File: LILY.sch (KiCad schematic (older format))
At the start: 8 parts

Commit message: LILY notitzen hinzugefügt
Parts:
- added C?: C, symbol C
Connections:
- net labels added: +3.3V, HOST_WKUP, POWER_DOWN-N, SDIO_EN-N, WAKE_UP
- wire segments 18 -> 24
- no-connect marks 6 -> 8
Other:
- note added: "Output wake up signal to host. \n\n"
- note added: "Pin is also used by USB as USB_VBUS_ON: \nUSB VBus On, USB power valid indication. \n"
- note added: "USB/SDIO-n :High level activates the USB interface. Internal pull-up (USB is default). Notice 1.8 V pin. \n"
- note added: "Wake up input signal. Active high .Notice 1.8 V pin. \n\n\n"
- moved on the sheet: C?, R?, U?
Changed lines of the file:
@@
 L R R?
 U 1 1 57112774
-P 6050 3950
-F 0 "R?" V 6130 3950 50  0000 C CNN
-F 1 "R" V 5975 3950 50  0000 C CNN
-F 2 "" V 5980 3950 30  0000 C CNN
-F 3 "" H 6050 3950 30  0000 C CNN
-	1    6050 3950
+P 6050 4100
+F 0 "R?" V 6130 4100 50  0000 C CNN
+F 1 "R" V 5975 4100 50  0000 C CNN
+F 2 "" V 5980 4100 30  0000 C CNN
+F 3 "" H 6050 4100 30  0000 C CNN
+	1    6050 4100
 	0    1    1    0
 $EndComp
@@
 L R R?
 U 1 1 571127A8
-P 5450 4050
-F 0 "R?" V 5530 4050 50  0000 C CNN
-F 1 "R" V 5375 4050 50  0000 C CNN
-F 2 "" V 5380 4050 30  0000 C CNN
-F 3 "" H 5450 4050 30  0000 C CNN
-	1    5450 4050
+P 5450 4200
+F 0 "R?" V 5530 4200 50  0000 C CNN
+F 1 "R" V 5375 4200 50  0000 C CNN
+F 2 "" V 5380 4200 30  0000 C CNN
+F 3 "" H 5450 4200 30  0000 C CNN
+	1    5450 4200
 	0    1    1    0
 $EndComp
@@
 L C C?
 U 1 1 571127D2
-P 6400 4450
-F 0 "C?" H 6450 4550 50  0000 L CNN
-F 1 "C" H 6450 4350 50  0000 L CNN
-F 2 "" H 6438 4300 30  0000 C CNN
-F 3 "" H 6450 4550 60  0000 C CNN
-	1    6400 4450
+P 6400 4600
+F 0 "C?" H 6450 4700 50  0000 L CNN
+F 1 "C" H 6450 4500 50  0000 L CNN
+F 2 "" H 6438 4450 30  0000 C CNN
+F 3 "" H 6450 4700 60  0000 C CNN
+	1    6400 4600
 	1    0    0    -1
 $EndComp
@@
 L C C?
 U 1 1 571127FC
-P 6800 4450
-F 0 "C?" H 6850 4550 50  0000 L CNN
-F 1 "C" H 6850 4350 50  0000 L CNN
-F 2 "" H 6838 4300 30  0000 C CNN
-F 3 "" H 6850 4550 60  0000 C CNN
-	1    6800 4450
-	1    0    0    -1
-$EndComp
-Wire Wire Line
-	4900 3950 5850 3950
-Wire Wire Line
-	5250 4050 4900 4050
-Wire Wire Line
-	5650 4050 7150 4050
-Wire Wire Line
-	6400 4050 6400 4250
-Wire Wire Line
-	6250 3950 7150 3950
-Wire Wire Line
-	6800 3950 6800 4250
-Connection ~ 6400 4050
-Connection ~ 6800 3950
+P 6800 4600
+F 0 "C?" H 6850 4700 50  0000 L CNN
+F 1 "C" H 6850 4500 50  0000 L CNN
+F 2 "" H 6838 4450 30  0000 C CNN
+F 3 "" H 6850 4700 60  0000 C CNN
+	1    6800 4600
+	1    0    0    -1
+$EndComp
+Wire Wire Line
+	4900 4100 5850 4100
+Wire Wire Line
+	5250 4200 4900 4200
+Wire Wire Line
+	5650 4200 7150 4200
+Wire Wire Line
+	6400 4200 6400 4400
+Wire Wire Line
+	6250 4100 7150 4100
+Wire Wire Line
+	6800 4100 6800 4400
+Connection ~ 6400 4200
+Connection ~ 6800 4100
 $Comp
 L GND #PWR?
 U 1 1 57112915
-P 6800 4800
-F 0 "#PWR?" H 6800 4550 50  0001 C CNN
-F 1 "GND" H 6800 4650 50  0000 C CNN
-F 2 "" H 6800 4800 50  0000 C CNN
-F 3 "" H 6800 4800 50  0000 C CNN
-	1    6800 4800
+P 6800 4950
+F 0 "#PWR?" H 6800 4700 50  0001 C CNN
+F 1 "GND" H 6800 4800 50  0000 C CNN
+F 2 "" H 6800 4950 50  0000 C CNN
+F 3 "" H 6800 4950 50  0000 C CNN
+	1    6800 4950
 	1    0    0    -1
 $EndComp
@@
 L GND #PWR?
 U 1 1 5711293E
-P 6400 4800
-F 0 "#PWR?" H 6400 4550 50  0001 C CNN
-F 1 "GND" H 6400 4650 50  0000 C CNN
-F 2 "" H 6400 4800 50  0000 C CNN
-F 3 "" H 6400 4800 50  0000 C CNN
-	1    6400 4800
-	1    0    0    -1
-$EndComp
-Wire Wire Line
-	6800 4800 6800 4650
-Wire Wire Line
-	6400 4650 6400 4800
-Text HLabel 7150 4050 2    60   Input ~ 0
+P 6400 4950
+F 0 "#PWR?" H 6400 4700 50  0001 C CNN
+F 1 "GND" H 6400 4800 50  0000 C CNN
+F 2 "" H 6400 4950 50  0000 C CNN
+F 3 "" H 6400 4950 50  0000 C CNN
+	1    6400 4950
+	1    0    0    -1
+$EndComp
+Wire Wire Line
+	6800 4950 6800 4800
+Wire Wire Line
+	6400 4800 6400 4950
+Text HLabel 7150 4200 2    60   Input ~ 0
 USB_D+
-Text HLabel 7150 3950 2    60   Input ~ 0
+Text HLabel 7150 4100 2    60   Input ~ 0
 USB_D-
 $Comp
 L AS179-92LF U?
 U 1 1 57112CC8
-P 7800 2850
-F 0 "U?" H 8050 2600 60  0000 C CNN
-F 1 "AS179-92LF" H 7800 3100 60  0000 C CNN
-F 2 "" H 7850 2850 60  0000 C CNN
-F 3 "" H 7850 2850 60  0000 C CNN
-	1    7800 2850
+P 8600 3300
+F 0 "U?" H 8850 3050 60  0000 C CNN
+F 1 "AS179-92LF" H 8600 3550 60  0000 C CNN
+F 2 "" H 8650 3300 60  0000 C CNN
+F 3 "" H 8650 3300 60  0000 C CNN
+	1    8600 3300
 	1    0    0    -1
 $EndComp
@@
 L R R?
 U 1 1 57112D8E
-P 6050 2700
-F 0 "R?" V 6130 2700 50  0000 C CNN
-F 1 "R" V 5975 2700 50  0000 C CNN
-F 2 "" V 5980 2700 30  0000 C CNN
-F 3 "" H 6050 2700 30  0000 C CNN
-	1    6050 2700
+P 6850 3150
+F 0 "R?" V 6930 3150 50  0000 C CNN
+F 1 "R" V 6775 3150 50  0000 C CNN
+F 2 "" V 6780 3150 30  0000 C CNN
+F 3 "" H 6850 3150 30  0000 C CNN
+	1    6850 3150
 	0    1    1    0
 $EndComp
@@
 L R R?
 U 1 1 57112DE1
-P 6500 2850
-F 0 "R?" V 6580 2850 50  0000 C CNN
-F 1 "R" V 6425 2850 50  0000 C CNN
-F 2 "" V 6430 2850 30  0000 C CNN
-F 3 "" H 6500 2850 30  0000 C CNN
-	1    6500 2850
-	0    1    1    0
-$EndComp
-Wire Wire Line
-	7300 2700 6250 2700
-Wire Wire Line
-	6700 2850 7300 2850
-Wire Wire Line
-	4900 3100 5650 3100
-Wire Wire Line
-	5650 3100 5650 2700
-Wire Wire Line
-	5650 2700 5850 2700
-Wire Wire Line
-	4900 3200 5750 3200
-Wire Wire Line
-	5750 3200 5750 2850
-Wire Wire Line
-	5750 2850 6300 2850
+P 7300 3300
+F 0 "R?" V 7380 3300 50  0000 C CNN
+F 1 "R" V 7225 3300 50  0000 C CNN
+F 2 "" V 7230 3300 30  0000 C CNN
+F 3 "" H 7300 3300 30  0000 C CNN
+	1    7300 3300
+	0    1    1    0
+$EndComp
+Wire Wire Line
+	8100 3150 7050 3150
+Wire Wire Line
+	7500 3300 8100 3300
+Wire Wire Line
+	4900 3250 5650 3250
+Wire Wire Line
+	4900 3350 5750 3350
+Text HLabel 2650 2550 0    60   Input ~ 0
+WAKE_UP
+Text HLabel 2650 2650 0    60   Input ~ 0
+HOST_WKUP
+Wire Wire Line
+	2650 2550 2900 2550
+Wire Wire Line
+	2650 2650 2900 2650
+Text HLabel 5200 3800 2    60   Input ~ 0
+SDIO_EN-N
+Text HLabel 5200 3900 2    60   Input ~ 0
+POWER_DOWN-N
+$Comp
+L +3.3V #PWR?
+U 1 1 57149C0A
+P 5700 1850
+F 0 "#PWR?" H 5700 1700 50  0001 C CNN
+F 1 "+3.3V" H 5700 1990 50  0000 C CNN
+F 2 "" H 5700 1850 50  0000 C CNN
+F 3 "" H 5700 1850 50  0000 C CNN
+	1    5700 1850
+	1    0    0    -1
+$EndComp
+Wire Wire Line
+	4900 3800 5200 3800
+Wire Wire Line
+	4900 3900 5200 3900
+$Comp
+L GND #PWR?
+U 1 1 5714A025
+P 5700 2800
+F 0 "#PWR?" H 5700 2550 50  0001 C CNN
+F 1 "GND" H 5700 2650 50  0000 C CNN
+F 2 "" H 5700 2800 50  0000 C CNN
+F 3 "" H 5700 2800 50  0000 C CNN
+	1    5700 2800
+	1    0    0    -1
+$EndComp
+$Comp
+L C C?
+U 1 1 5714A0A3
+P 5700 2350
+F 0 "C?" H 5750 2450 50  0000 L CNN
+F 1 "C" H 5750 2250 50  0000 L CNN
+F 2 "" H 5738 2200 30  0000 C CNN
+F 3 "" H 5750 2450 60  0000 C CNN
+	1    5700 2350
+	1    0    0    -1
+$EndComp
+Wire Wire Line
+	4900 2550 5350 2550
+Wire Wire Line
+	5350 1950 5350 2650
+Wire Wire Line
+	5350 1950 5700 1950
+Wire Wire Line
+	5700 1850 5700 2150
+Connection ~ 5700 1950
+Wire Wire Line
+	5700 2800 5700 2550
+Wire Wire Line
+	5350 2650 4900 2650
+Connection ~ 5350 2550
+Text Notes 6000 3800 0    60   ~ 0
+USB/SDIO-n :High level activates the USB interface. Internal pull-up (USB is default). Notice 1.8 V pin. \n
+NoConn ~ 4900 3550
+NoConn ~ 4900 3650
+Text Notes 650  2600 0    60   ~ 0
+Wake up input signal. Active high .Notice 1.8 V pin. \n\n\n
+Text Notes 550  2800 0    60   ~ 0
+Output wake up signal to host. \n\n
+Text Notes 750  3800 0    60   ~ 0
+Pin is also used by USB as USB_VBUS_ON: \nUSB VBus On, USB power valid indication. \n
 $EndSCHEMATC

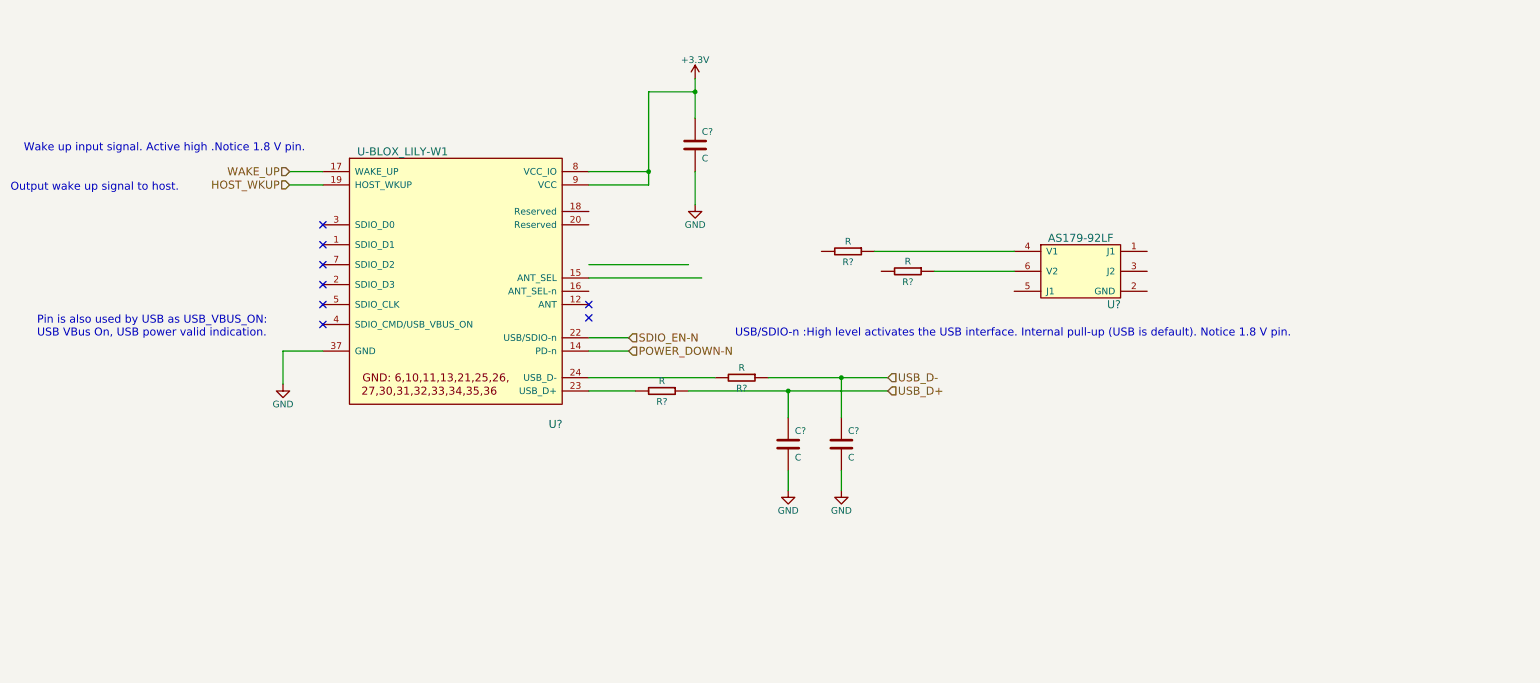
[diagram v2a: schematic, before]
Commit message: 3V8 footprints ergänzt
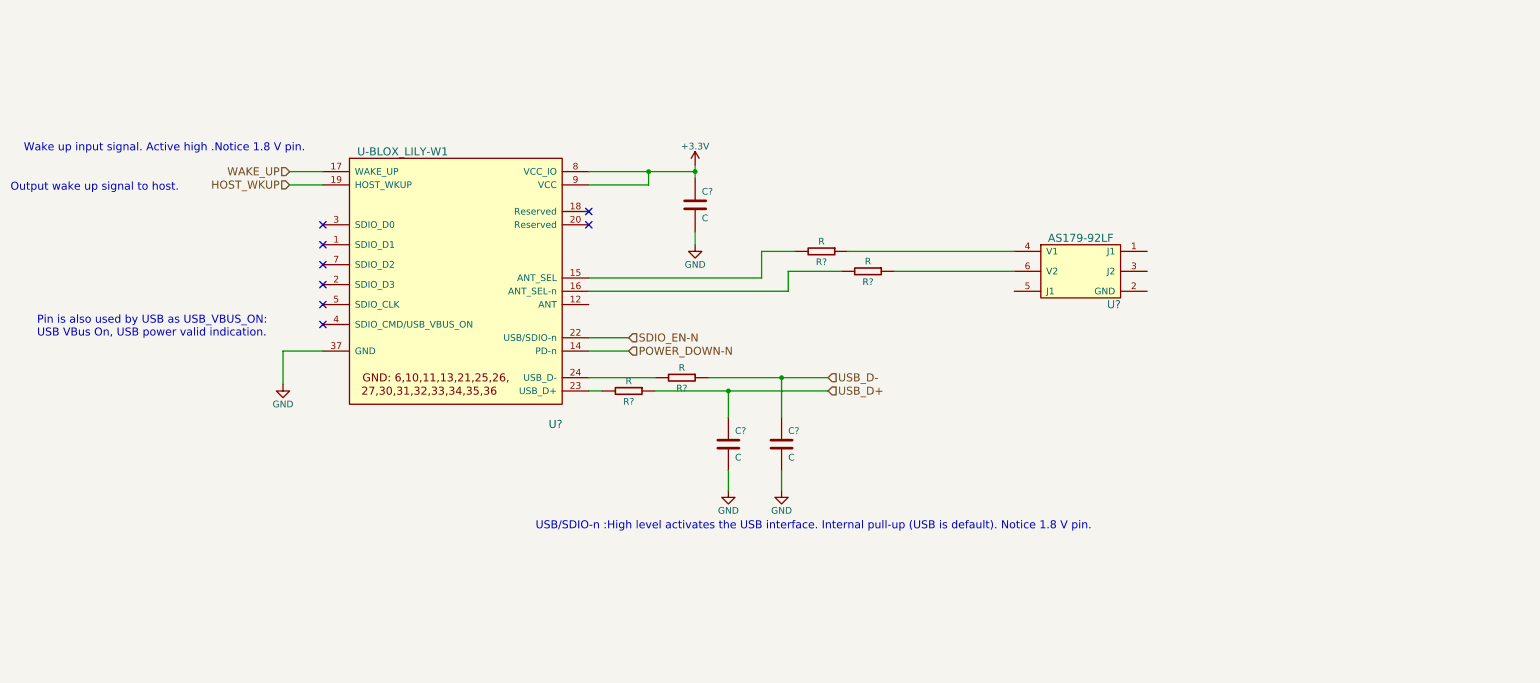
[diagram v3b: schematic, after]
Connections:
- wire segments 24 -> 27
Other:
- moved on the sheet: C?, R?
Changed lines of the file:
@@
 L R R?
 U 1 1 57112774
-P 6050 4100
-F 0 "R?" V 6130 4100 50  0000 C CNN
-F 1 "R" V 5975 4100 50  0000 C CNN
-F 2 "" V 5980 4100 30  0000 C CNN
-F 3 "" H 6050 4100 30  0000 C CNN
-	1    6050 4100
+P 5600 4100
+F 0 "R?" V 5680 4100 50  0000 C CNN
+F 1 "R" V 5525 4100 50  0000 C CNN
+F 2 "" V 5530 4100 30  0000 C CNN
+F 3 "" H 5600 4100 30  0000 C CNN
+	1    5600 4100
 	0    1    1    0
 $EndComp
@@
 L R R?
 U 1 1 571127A8
-P 5450 4200
-F 0 "R?" V 5530 4200 50  0000 C CNN
-F 1 "R" V 5375 4200 50  0000 C CNN
-F 2 "" V 5380 4200 30  0000 C CNN
-F 3 "" H 5450 4200 30  0000 C CNN
-	1    5450 4200
+P 5200 4200
+F 0 "R?" V 5280 4200 50  0000 C CNN
+F 1 "R" V 5125 4200 50  0000 C CNN
+F 2 "" V 5130 4200 30  0000 C CNN
+F 3 "" H 5200 4200 30  0000 C CNN
+	1    5200 4200
 	0    1    1    0
 $EndComp
@@
 L C C?
 U 1 1 571127D2
-P 6400 4600
-F 0 "C?" H 6450 4700 50  0000 L CNN
-F 1 "C" H 6450 4500 50  0000 L CNN
-F 2 "" H 6438 4450 30  0000 C CNN
-F 3 "" H 6450 4700 60  0000 C CNN
-	1    6400 4600
+P 5950 4600
+F 0 "C?" H 6000 4700 50  0000 L CNN
+F 1 "C" H 6000 4500 50  0000 L CNN
+F 2 "" H 5988 4450 30  0000 C CNN
+F 3 "" H 6000 4700 60  0000 C CNN
+	1    5950 4600
 	1    0    0    -1
 $EndComp
@@
 L C C?
 U 1 1 571127FC
-P 6800 4600
-F 0 "C?" H 6850 4700 50  0000 L CNN
-F 1 "C" H 6850 4500 50  0000 L CNN
-F 2 "" H 6838 4450 30  0000 C CNN
-F 3 "" H 6850 4700 60  0000 C CNN
-	1    6800 4600
-	1    0    0    -1
-$EndComp
-Wire Wire Line
-	4900 4100 5850 4100
-Wire Wire Line
-	5250 4200 4900 4200
-Wire Wire Line
-	5650 4200 7150 4200
-Wire Wire Line
-	6400 4200 6400 4400
-Wire Wire Line
-	6250 4100 7150 4100
-Wire Wire Line
-	6800 4100 6800 4400
-Connection ~ 6400 4200
-Connection ~ 6800 4100
+P 6350 4600
+F 0 "C?" H 6400 4700 50  0000 L CNN
+F 1 "C" H 6400 4500 50  0000 L CNN
+F 2 "" H 6388 4450 30  0000 C CNN
+F 3 "" H 6400 4700 60  0000 C CNN
+	1    6350 4600
+	1    0    0    -1
+$EndComp
+Wire Wire Line
+	5950 4200 5950 4400
+Wire Wire Line
+	5800 4100 6700 4100
+Wire Wire Line
+	6350 4100 6350 4400
+Connection ~ 5950 4200
+Connection ~ 6350 4100
 $Comp
 L GND #PWR?
 U 1 1 57112915
-P 6800 4950
-F 0 "#PWR?" H 6800 4700 50  0001 C CNN
-F 1 "GND" H 6800 4800 50  0000 C CNN
-F 2 "" H 6800 4950 50  0000 C CNN
-F 3 "" H 6800 4950 50  0000 C CNN
-	1    6800 4950
+P 6350 4950
+F 0 "#PWR?" H 6350 4700 50  0001 C CNN
+F 1 "GND" H 6350 4800 50  0000 C CNN
+F 2 "" H 6350 4950 50  0000 C CNN
+F 3 "" H 6350 4950 50  0000 C CNN
+	1    6350 4950
 	1    0    0    -1
 $EndComp
@@
 L GND #PWR?
 U 1 1 5711293E
-P 6400 4950
-F 0 "#PWR?" H 6400 4700 50  0001 C CNN
-F 1 "GND" H 6400 4800 50  0000 C CNN
-F 2 "" H 6400 4950 50  0000 C CNN
-F 3 "" H 6400 4950 50  0000 C CNN
-	1    6400 4950
-	1    0    0    -1
-$EndComp
-Wire Wire Line
-	6800 4950 6800 4800
-Wire Wire Line
-	6400 4800 6400 4950
-Text HLabel 7150 4200 2    60   Input ~ 0
+P 5950 4950
+F 0 "#PWR?" H 5950 4700 50  0001 C CNN
+F 1 "GND" H 5950 4800 50  0000 C CNN
+F 2 "" H 5950 4950 50  0000 C CNN
+F 3 "" H 5950 4950 50  0000 C CNN
+	1    5950 4950
+	1    0    0    -1
+$EndComp
+Wire Wire Line
+	6350 4950 6350 4800
+Wire Wire Line
+	5950 4800 5950 4950
+Text HLabel 6700 4200 2    60   Input ~ 0
 USB_D+
-Text HLabel 7150 4100 2    60   Input ~ 0
+Text HLabel 6700 4100 2    60   Input ~ 0
 USB_D-
 $Comp
@@
 L R R?
 U 1 1 57112D8E
-P 6850 3150
-F 0 "R?" V 6930 3150 50  0000 C CNN
-F 1 "R" V 6775 3150 50  0000 C CNN
-F 2 "" V 6780 3150 30  0000 C CNN
-F 3 "" H 6850 3150 30  0000 C CNN
-	1    6850 3150
+P 6650 3150
+F 0 "R?" V 6730 3150 50  0000 C CNN
+F 1 "R" V 6575 3150 50  0000 C CNN
+F 2 "" V 6580 3150 30  0000 C CNN
+F 3 "" H 6650 3150 30  0000 C CNN
+	1    6650 3150
 	0    1    1    0
 $EndComp
@@
 L R R?
 U 1 1 57112DE1
-P 7300 3300
-F 0 "R?" V 7380 3300 50  0000 C CNN
-F 1 "R" V 7225 3300 50  0000 C CNN
-F 2 "" V 7230 3300 30  0000 C CNN
-F 3 "" H 7300 3300 30  0000 C CNN
-	1    7300 3300
-	0    1    1    0
-$EndComp
-Wire Wire Line
-	8100 3150 7050 3150
-Wire Wire Line
-	7500 3300 8100 3300
-Wire Wire Line
-	4900 3250 5650 3250
-Wire Wire Line
-	4900 3350 5750 3350
+P 7000 3300
+F 0 "R?" V 7080 3300 50  0000 C CNN
+F 1 "R" V 6925 3300 50  0000 C CNN
+F 2 "" V 6930 3300 30  0000 C CNN
+F 3 "" H 7000 3300 30  0000 C CNN
+	1    7000 3300
+	0    1    1    0
+$EndComp
+Wire Wire Line
+	6850 3150 8100 3150
+Wire Wire Line
+	7200 3300 8100 3300
 Text HLabel 2650 2550 0    60   Input ~ 0
 WAKE_UP
@@
 L +3.3V #PWR?
 U 1 1 57149C0A
-P 5700 1850
-F 0 "#PWR?" H 5700 1700 50  0001 C CNN
-F 1 "+3.3V" H 5700 1990 50  0000 C CNN
-F 2 "" H 5700 1850 50  0000 C CNN
-F 3 "" H 5700 1850 50  0000 C CNN
-	1    5700 1850
+P 5700 2500
+F 0 "#PWR?" H 5700 2350 50  0001 C CNN
+F 1 "+3.3V" H 5700 2640 50  0000 C CNN
+F 2 "" H 5700 2500 50  0000 C CNN
+F 3 "" H 5700 2500 50  0000 C CNN
+	1    5700 2500
 	1    0    0    -1
 $EndComp
@@
 L GND #PWR?
 U 1 1 5714A025
-P 5700 2800
-F 0 "#PWR?" H 5700 2550 50  0001 C CNN
-F 1 "GND" H 5700 2650 50  0000 C CNN
-F 2 "" H 5700 2800 50  0000 C CNN
-F 3 "" H 5700 2800 50  0000 C CNN
-	1    5700 2800
+P 5700 3100
+F 0 "#PWR?" H 5700 2850 50  0001 C CNN
+F 1 "GND" H 5700 2950 50  0000 C CNN
+F 2 "" H 5700 3100 50  0000 C CNN
+F 3 "" H 5700 3100 50  0000 C CNN
+	1    5700 3100
 	1    0    0    -1
 $EndComp
@@
 L C C?
 U 1 1 5714A0A3
-P 5700 2350
-F 0 "C?" H 5750 2450 50  0000 L CNN
-F 1 "C" H 5750 2250 50  0000 L CNN
-F 2 "" H 5738 2200 30  0000 C CNN
-F 3 "" H 5750 2450 60  0000 C CNN
-	1    5700 2350
-	1    0    0    -1
-$EndComp
-Wire Wire Line
-	4900 2550 5350 2550
-Wire Wire Line
-	5350 1950 5350 2650
-Wire Wire Line
-	5350 1950 5700 1950
-Wire Wire Line
-	5700 1850 5700 2150
-Connection ~ 5700 1950
-Wire Wire Line
-	5700 2800 5700 2550
+P 5700 2800
+F 0 "C?" H 5750 2900 50  0000 L CNN
+F 1 "C" H 5750 2700 50  0000 L CNN
+F 2 "" H 5738 2650 30  0000 C CNN
+F 3 "" H 5750 2900 60  0000 C CNN
+	1    5700 2800
+	1    0    0    -1
+$EndComp
+Wire Wire Line
+	4900 2550 5700 2550
 Wire Wire Line
 	5350 2650 4900 2650
 Connection ~ 5350 2550
-Text Notes 6000 3800 0    60   ~ 0
+Text Notes 4500 5250 0    60   ~ 0
 USB/SDIO-n :High level activates the USB interface. Internal pull-up (USB is default). Notice 1.8 V pin. \n
-NoConn ~ 4900 3550
-NoConn ~ 4900 3650
+NoConn ~ 4900 2850
+NoConn ~ 4900 2950
 Text Notes 650  2600 0    60   ~ 0
 Wake up input signal. Active high .Notice 1.8 V pin. \n\n\n
@@
 Text Notes 750  3800 0    60   ~ 0
 Pin is also used by USB as USB_VBUS_ON: \nUSB VBus On, USB power valid indication. \n
+Wire Wire Line
+	6700 4200 5400 4200
+Wire Wire Line
+	5400 4100 4900 4100
+Wire Wire Line
+	5000 4200 4900 4200
+Wire Wire Line
+	4900 3350 6200 3350
+Wire Wire Line
+	6200 3350 6200 3150
+Wire Wire Line
+	4900 3450 6400 3450
+Wire Wire Line
+	6400 3450 6400 3300
+Wire Wire Line
+	5700 2500 5700 2600
+Connection ~ 5700 2550
+Wire Wire Line
+	5350 2650 5350 2550
+Wire Wire Line
+	5700 3000 5700 3100
+Wire Wire Line
+	6200 3150 6450 3150
+Wire Wire Line
+	6400 3300 6800 3300
 $EndSCHEMATC

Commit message: LILY Antenne hinzugefügt
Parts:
- added C? (x8): C, symbol C
- added R?: 33k, Passives:R0402N, symbol R
- added X?: ANT, symbol ANT
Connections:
- net +3V3: now also C?.1, C?.1, C?.1, R?.2
- net GND: now also C?.2, C?.2, C?.2, C?.2, C?.2, C?.2, C?.2, X?.P (GND)
- net at U?.12 (ANT): now also C?.1, C?.2
- net at U?.4 (SDIO_CMD/USB_VBUS_ON): now also R?.1
- net at R?.1, U?.4 (V1): now also C?.1
- net at R?.1, U?.6 (V2): now also C?.1
- net SDIO_EN-N: no longer names the net of U?.22 (USB/SDIO-n)
- new net: C?.1, C?.1, X?.1 (SIG)
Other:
- note added: "Connect to VCC through a 33 kΩ resistor"
- note added: "USB mode (USB/SDIO-n pin not connected)"
- note added: "\nA minimum bulk capacitance of 10 μF on VCC rail is required close to the module to help f\nilter current spikes from the RF section. \nKein in EVK-LILY-W1 !"

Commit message: added some footprints
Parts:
- removed C? (x5): C, symbol C
- removed R?: R, symbol R
- added C401, C402, C403, C405: 10p, Passives:C0402N, symbol C
- added C404: 100n, Passives:C0402N, symbol C
- added R402: 0, Passives:R0402N, symbol R
- C406: renamed from C?; value C -> 2.2u; footprint (none) -> Passives:C1206N
- C409, C411: renamed from C?; footprint (none) -> Passives:C0402N
- C410: renamed from C?; value C -> 10p; footprint (none) -> Passives:C0402N
- R403: renamed from R?; value R -> 0; footprint (none) -> Passives:R0402N
- X401: renamed from X?; footprint (none) -> Connector:U.FL-R-SMT
- gave numbers to parts that had none: 7
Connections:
- net +3V3: now also C406.2, C401.2, C403.2, C404.2; no longer C406.1
- net GND: now also C406.1, C401.1, C402.1, C403.1, C404.1, C405.1; no longer C406.2
- net USB_D+: now also C402.2, R402.1
- net USB_D-: now also C405.2
- net at U401.23 (USB_D+): now also R402.2
